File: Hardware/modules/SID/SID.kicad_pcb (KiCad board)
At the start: 4 copper layers, 83.3 x 68.2 mm, 19 parts, among them J1 Bus_PCI_6502, J2 POT_X, J3 POT_Y, J4 POT_X, U1 74HC138, U2 8580

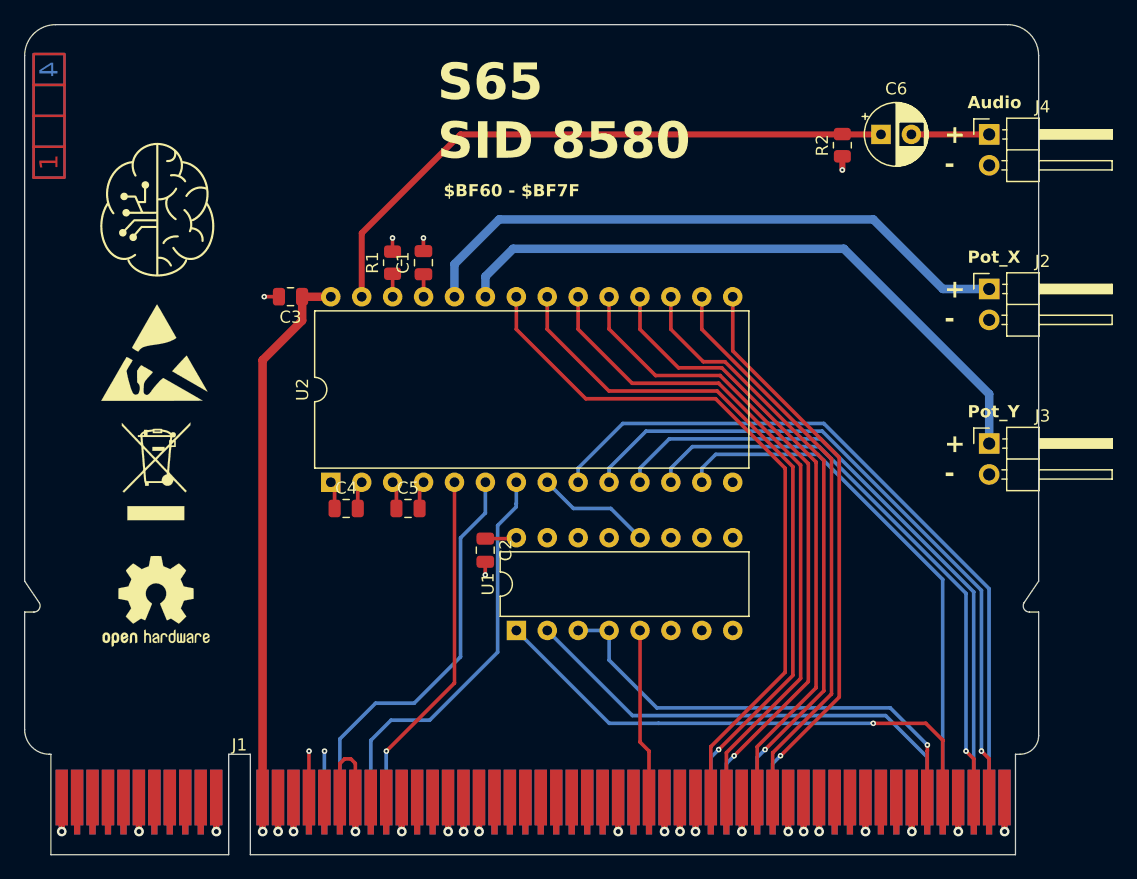
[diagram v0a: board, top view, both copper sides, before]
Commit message: Hardware Review Pt. 1 fix Address Decoding for Strobe Generators add bulk capacitance to every board fix wiring of Prototyping Board
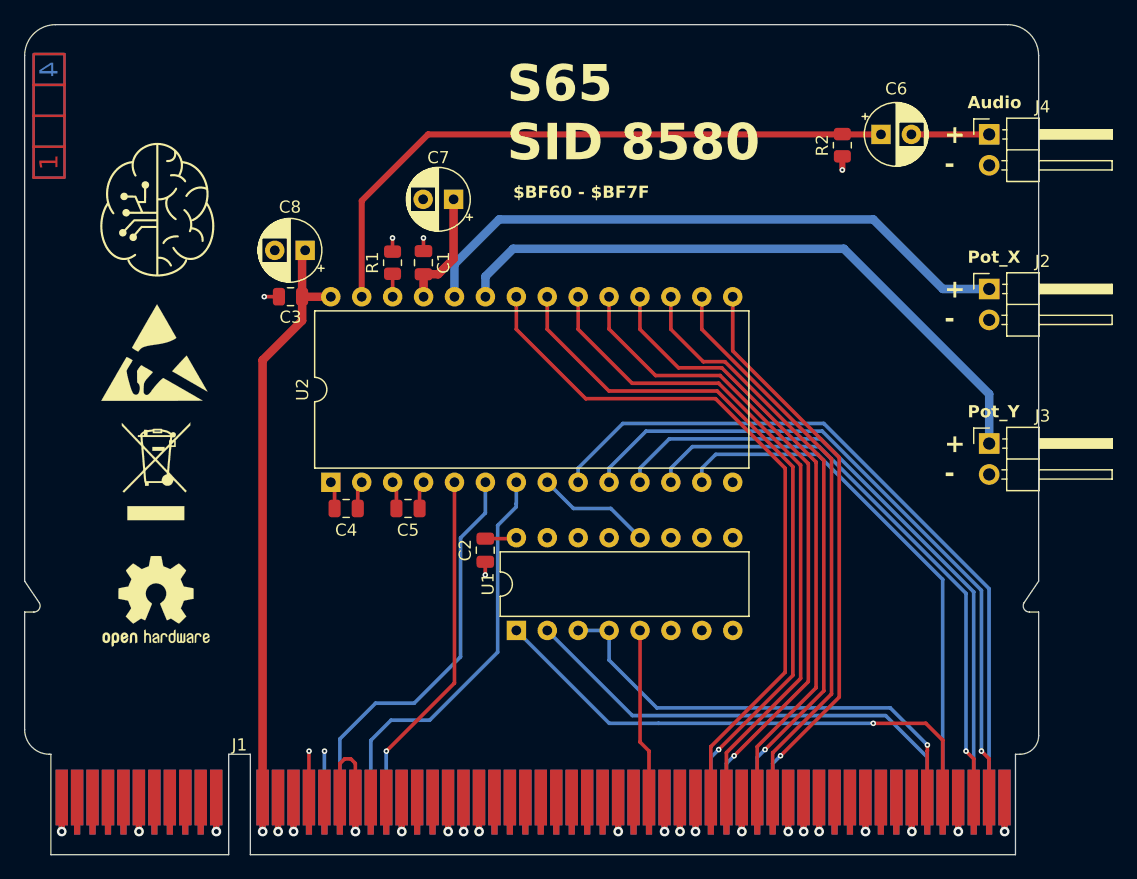
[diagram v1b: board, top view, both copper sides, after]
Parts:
- added C7: 10µ, Capacitor_THT:CP_Radial_D5.0mm_P2.50mm, F.Cu at (147.4, 60.5)
- added C8: 10µ, Capacitor_THT:CP_Radial_D5.0mm_P2.50mm, F.Cu at (135.2, 64.6)
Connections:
- J1 pad A11: /A13 -> unconnected-(J1-A13-PadA11)_0
- J1 pad A12: /A15 -> unconnected-(J1-A15-PadA12)
- J1 pad A25: /~{ROM} -> unconnected-(J1-~{ROM}-PadA25)
- J1 pad A27: /~{IRQ_0.0} -> unconnected-(J1-~{IRQ_0.0}-PadA27)_0
- J1 pad A28: /~{IRQ_0.1} -> unconnected-(J1-~{IRQ_0.1}-PadA28)
- J1 pad A29: /~{IRQ_0.2} -> unconnected-(J1-~{IRQ_0.2}-PadA29)_0
- J1 pad A30: /~{IRQ_0.3} -> unconnected-(J1-~{IRQ_0.3}-PadA30)_0
- J1 pad A31: /~{IRQ_0.4} -> unconnected-(J1-~{IRQ_0.4}-PadA31)
- J1 pad A32: /~{IRQ_0.5} -> unconnected-(J1-~{IRQ_0.5}-PadA32)
- J1 pad A33: /~{IRQ_0.6} -> unconnected-(J1-~{IRQ_0.6}-PadA33)
- J1 pad A34: /~{IRQ_0.7} -> unconnected-(J1-~{IRQ_0.7}-PadA34)_0
- J1 pad A38: /SYNC_VPA -> unconnected-(J1-Sync/VPA-PadA38)
- J1 pad A39: /Ø2/VDA -> unconnected-(J1-Ø2/VDA-PadA39)
- J1 pad A41: /~{RDY} -> unconnected-(J1-~{RDY}-PadA41)_0
- J1 pad A42: /~{BE} -> unconnected-(J1-~{BE}-PadA42)_0
- J1 pad A45: /E -> unconnected-(J1-E-PadA45)_0
- J1 pad A53: /RAM_0 -> unconnected-(J1-RAM0-PadA53)_0
- J1 pad A54: /RAM_1 -> unconnected-(J1-RAM1-PadA54)_0
- J1 pad A55: /RAM_2 -> unconnected-(J1-RAM2-PadA55)_0
- J1 pad A56: /RAM_3 -> unconnected-(J1-RAM3-PadA56)_0
- J1 pad A58: /RAM_4 -> unconnected-(J1-RAM4-PadA58)_0
- J1 pad A59: /RAM_5 -> unconnected-(J1-RAM5-PadA59)_0
- J1 pad A60: /RAM_6 -> unconnected-(J1-RAM6-PadA60)_0
- J1 pad A61: /RAM_7 -> unconnected-(J1-RAM7-PadA61)_0
- J1 pad A8: /A9 -> unconnected-(J1-A9-PadA8)
- J1 pad A9: /A11 -> unconnected-(J1-A11-PadA9)
- J1 pad B11: /A12 -> unconnected-(J1-A12-PadB11)
- J1 pad B12: /A14 -> unconnected-(J1-A14-PadB12)_0
- J1 pad B24: /~{L_RAM} -> unconnected-(J1-~{L_RAM}-PadB24)
- J1 pad B25: /~{H_RAM} -> unconnected-(J1-~{H_RAM}-PadB25)_0
- J1 pad B27: /~{IRQ} -> unconnected-(J1-~{IRQ}-PadB27)_0
- J1 pad B28: /~{IRQ_0} -> unconnected-(J1-~{IRQ_0}-PadB28)
- J1 pad B29: /~{IRQ_1} -> unconnected-(J1-~{IRQ_1}-PadB29)_0
- J1 pad B30: /~{IRQ_2} -> unconnected-(J1-~{IRQ_2}-PadB30)_0
- J1 pad B31: /~{IRQ_3} -> unconnected-(J1-~{IRQ_3}-PadB31)
- J1 pad B32: /~{IRQ_4} -> unconnected-(J1-~{IRQ_4}-PadB32)_0
- J1 pad B33: /~{NMI} -> unconnected-(J1-~{NMI}-PadB33)_0
- J1 pad B34: /PAGE -> unconnected-(J1-PAGE_ROM-PadB34)_0
- J1 pad B38: /~{VP} -> unconnected-(J1-~{VP}-PadB38)
- J1 pad B39: /~{ML} -> unconnected-(J1-~{ML}-PadB39)_0
- J1 pad B46: /M/X -> unconnected-(J1-M/~{X}-PadB46)_0
- J1 pad B53: /ROM_0 -> unconnected-(J1-ROM0-PadB53)
- J1 pad B54: /ROM_1 -> unconnected-(J1-ROM1-PadB54)_0
- J1 pad B55: /ROM_2 -> unconnected-(J1-ROM2-PadB55)_0
- J1 pad B56: /ROM_3 -> unconnected-(J1-ROM3-PadB56)_0
- J1 pad B58: /ROM_4 -> unconnected-(J1-ROM4-PadB58)
- J1 pad B59: /ROM_5 -> unconnected-(J1-ROM5-PadB59)_0
- J1 pad B60: /ROM_6 -> unconnected-(J1-ROM6-PadB60)
- J1 pad B61: /ROM_7 -> unconnected-(J1-ROM7-PadB61)
- J1 pad B8: /A8 -> unconnected-(J1-A8-PadB8)
- J1 pad B9: /A10 -> unconnected-(J1-A10-PadB9)_0
- U1 pad 13: /PORT_64 -> unconnected-(U1-~{Y2}-Pad13)
- U1 pad 14: /PORT_32 -> unconnected-(U1-~{Y1}-Pad14)
- U1 pad 15: /PORT_0 -> unconnected-(U1-~{Y0}-Pad15)
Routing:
- net +5V: track 4.44 -> 12.3 mm
- net +9V: track 44.9 -> 48.8 mm
- net Net-(U2-AUDIO_OUT): track 51.2 -> 52.8 mm

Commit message: Big Review Update - Changed Copper Pours on all PCBs - Implemented errors found at review - fixed some additional errors
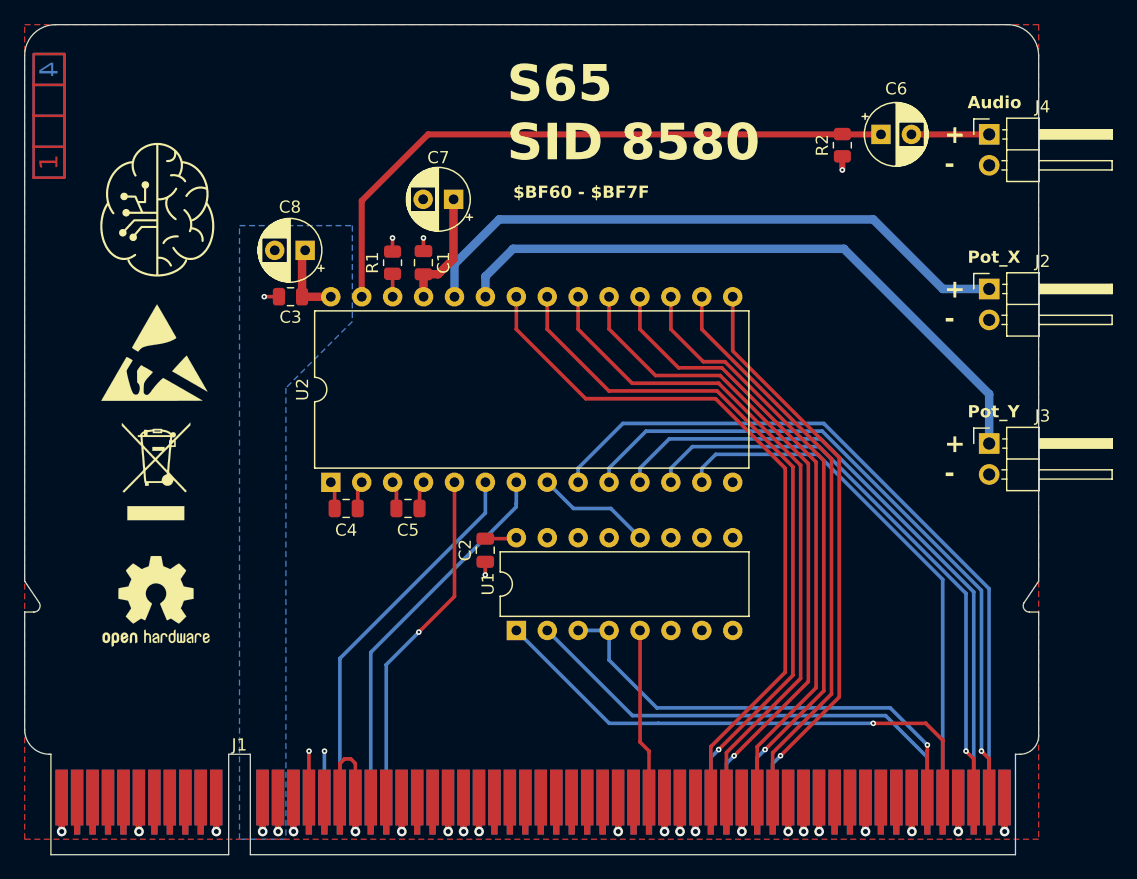
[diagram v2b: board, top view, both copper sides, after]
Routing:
- net +9V: track 48.8 -> 6.28 mm
- net /CLK: track 32.7 -> 30.9 mm
- net /R/~{W}: track 32.7 -> 30.9 mm
- added copper zone on F.Cu, net +5V
- added copper zone on B.Cu, net +9V
- added copper zone on In1.Cu, net GND
- removed copper zone on In1.Cu, net +5V
